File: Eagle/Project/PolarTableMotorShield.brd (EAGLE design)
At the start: 5 parts, among them U8 CD74HC4094M96

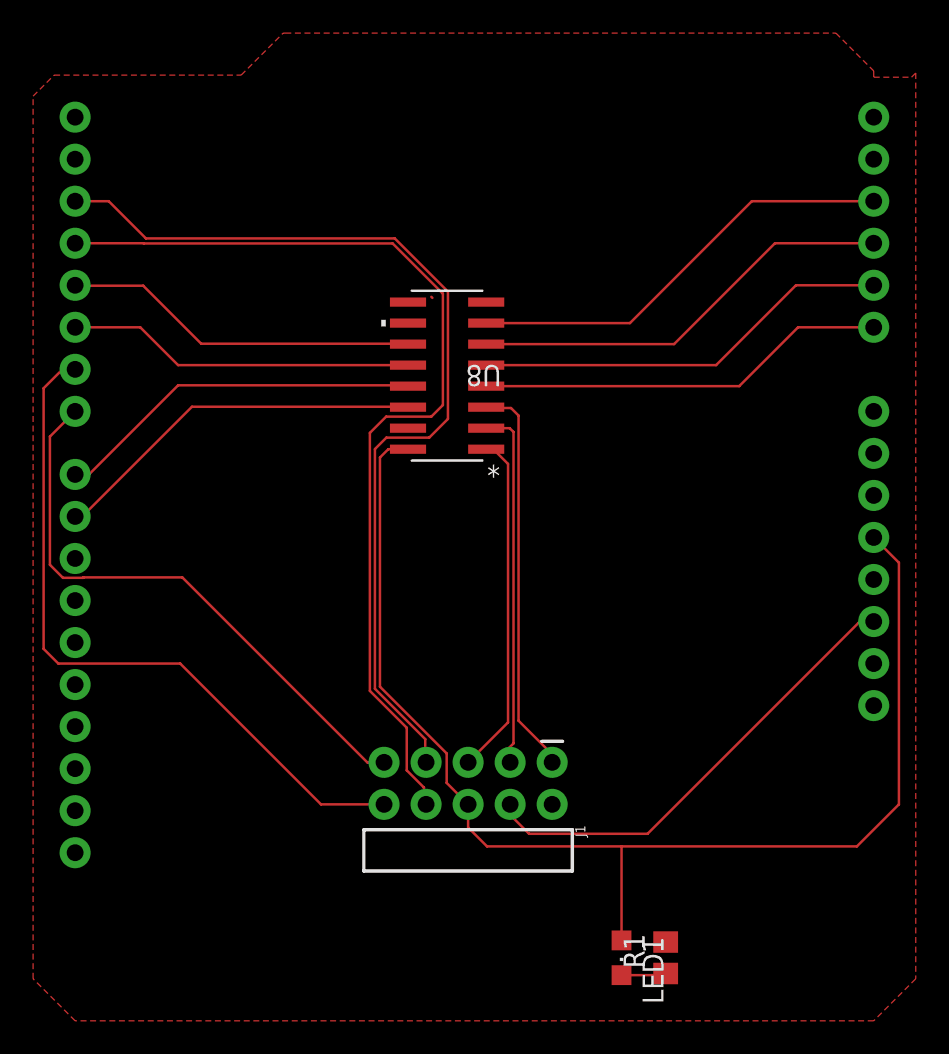
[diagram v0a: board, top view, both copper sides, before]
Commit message: Changed the connector to be 6x2 so the shift reg could run at 3.3V
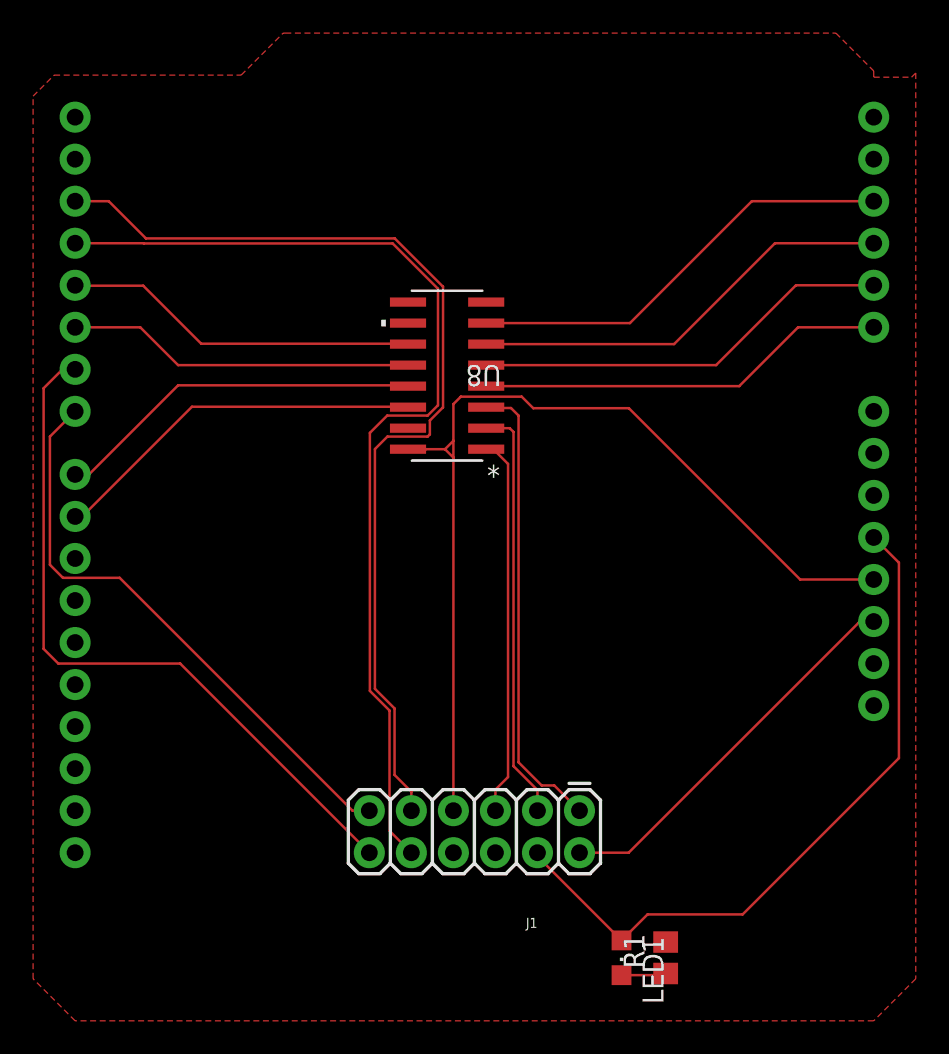
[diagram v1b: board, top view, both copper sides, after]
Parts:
- J1: device SparkFun-Connectors:2X5-RA -> keir_library:2X6
- moved J1 6.93 mm to (33.0, 12.7), turned to 180 degrees
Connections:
- new net VCC_2: B2.3.3V, J1.7, U8.16
- net !RES: now also J1.2; no longer J1.4
- net GND: now also J1.6, J1.8; no longer J1.2
- net VCC_1: now also J1.4; no longer J1.6, U8.16
- net XDIR: now also J1.10; no longer J1.8
- net XSTEP: now also J1.9; no longer J1.7
- net YDIR: now also J1.11; no longer J1.9
- net YSTEP: now also J1.12; no longer J1.10
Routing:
- net VCC_2: track 0.00 -> 61.2 mm
- net VCC_1: track 77.3 -> 43.5 mm
- net !RES: track 28.4 -> 23.6 mm
- net CLOCK: track 24.0 -> 28.0 mm
- net DATA: track 21.8 -> 25.2 mm
- net LATCH: track 20.7 -> 23.0 mm
- net XSTEP: track 57.9 -> 60.1 mm
- net XDIR: track 59.5 -> 61.3 mm
